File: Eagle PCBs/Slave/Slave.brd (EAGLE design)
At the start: 100 x 80 mm, 7 parts, among them Q1 TIP120

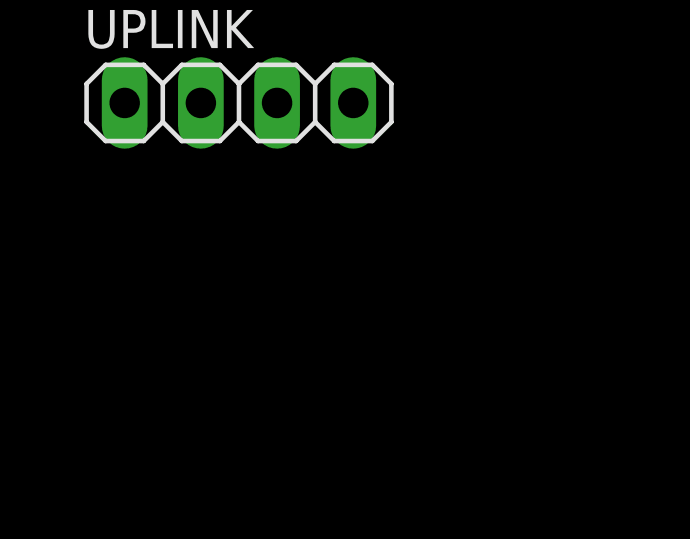
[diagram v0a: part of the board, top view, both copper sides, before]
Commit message: Added LED circuit to Slave PCB
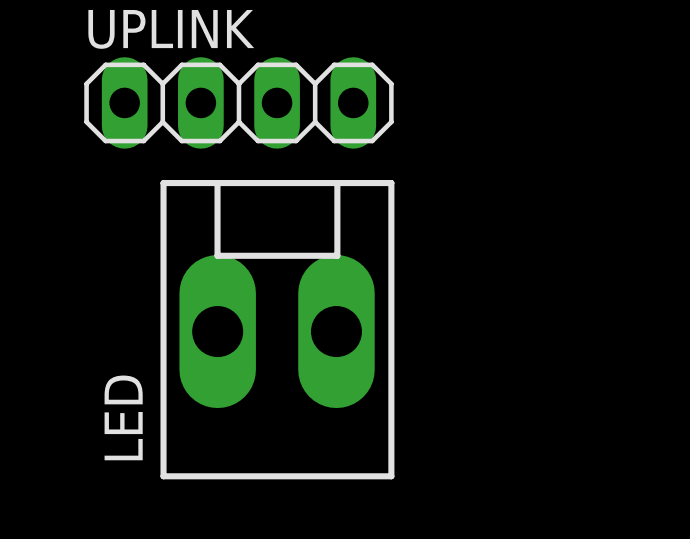
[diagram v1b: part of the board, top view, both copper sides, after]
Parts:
- added LED: (no value), con-molex:KK-156-2
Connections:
- net LED_GND: now also LED.2
- net VDD: now also LED.1
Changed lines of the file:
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@@
 <attribute name="VALUE" x="-26.67" y="-60.325" size="1.27" layer="27"/>
+</element>
+<element name="LED" library="con-molex" library_urn="urn:adsk.eagle:library:165" package="KK-156-2" package3d_urn="urn:adsk.eagle:package:8078800/1" value="" x="-20.32" y="-64.77" smashed="yes">
+<attribute name="MF" value="MOLEX" x="-20.32" y="-64.77" size="1.778" layer="27" display="off"/>
+<attribute name="MPN" value="" x="-20.32" y="-64.77" size="1.778" layer="27" display="off"/>
+<attribute name="NAME" x="-24.8" y="-69.215" size="1.27" layer="25" rot="R90"/>
+<attribute name="OC_FARNELL" value="unknown" x="-20.32" y="-64.77" size="1.778" layer="27" display="off"/>
+<attribute name="OC_NEWARK" value="unknown" x="-20.32" y="-64.77" size="1.778" layer="27" display="off"/>
+<attribute name="POPULARITY" value="10" x="-20.32" y="-64.77" size="1.778" layer="27" display="off"/>
+<attribute name="VALUE" x="-14.57" y="-69.215" size="1.27" layer="27" rot="R90"/>
 </element>
 </elements>
@@
 <signal name="LED_GND">
 <contactref element="Q1" pad="C"/>
+<contactref element="LED" pad="2"/>
+<wire x1="-21.59" y1="-33.02" x2="-18.34" y2="-64.77" width="0" layer="19" extent="1-1"/>
 </signal>
 <signal name="NANO_D3">
@@
 <signal name="VDD">
 <contactref element="UPLINK" pad="1"/>
+<contactref element="LED" pad="1"/>
+<wire x1="-25.4" y1="-57.15" x2="-22.3" y2="-64.77" width="0" layer="19" extent="1-1"/>
 </signal>
 </signals>
